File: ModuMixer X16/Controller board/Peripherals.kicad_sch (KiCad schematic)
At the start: 32 parts, among them J1 Screw_Terminal_01x05, J10 Conn_02x05_Counter_Clockwise, J11 Conn_02x06_Counter_Clockwise, J2 Screw_Terminal_01x03, J3 Screw_Terminal_01x05, J4 Screw_Terminal_01x03, J5 Screw_Terminal_01x05, J6 Screw_Terminal_01x05, Q1 MMBT2222A, SW1 Enter, SW10 SW_Push, SW11 SW_Push, SW12 SW_Push, SW13 RotaryEncoder_Switch_MP, SW14 RotaryEncoder_Switch_MP, SW15 RotaryEncoder_Switch_MP, SW16 SW_Push, SW17 SW_Push, SW18 SW_Push, SW19 SW_Push, SW2 Up, SW20 SW_Push, SW21 SW_Push, SW3 Down, SW4 Left, SW5 Right, SW6 RotaryEncoder_Switch_MP, SW7 RotaryEncoder_Switch_MP, SW8 SW_Push, SW9 SW_Push

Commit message: update idk
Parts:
- removed J1, J5, J6: Screw_Terminal_01x05, TerminalBlock:TerminalBlock_Xinya_XY308-2.54-5P_1x05_P2.54mm_Horizontal, symbol Connector:Screw_Terminal_01x05
- removed J4: Screw_Terminal_01x03, TerminalBlock:TerminalBlock_Xinya_XY308-2.54-3P_1x03_P2.54mm_Horizontal, symbol Connector:Screw_Terminal_01x03
- added J5: Conn_02x07_Counter_Clockwise, Connector_IDC:IDC-Header_2x07_P2.54mm_Vertical, symbol Connector_Generic:Conn_02x07_Counter_Clockwise
- added JP10, JP11: SolderJumper_2_Bridged, Jumper:SolderJumper-2_P1.3mm_Bridged2Bar_Pad1.0x1.5mm, symbol Jumper:SolderJumper_2_Bridged
- renumbered J2 to J1, J3 to J2, J10 to J3, J11 to J4
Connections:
- net GND: now also J5.2 (Pin_2)
- net MAIN_OUT_L_P: now also JP10.2 (B)
- net MAIN_OUT_R_P: now also JP11.1 (A)
- net M_USART_CLK: now also J5.6 (Pin_6)
- net M_USART_RX: now also J5.5 (Pin_5)
- net M_USART_TX: now also J5.4 (Pin_4)
- net READY: now also J5.3 (Pin_3)
- new net 12V_MOD: J5.1 (Pin_1)
- new net CUE_LM: J5.10 (Pin_10)
- new net CUE_LP: J5.9 (Pin_9)
- new net CUE_RM: J5.8 (Pin_8)
- new net CUE_RP: J5.7 (Pin_7)
- new net MAIN_LM: J5.14 (Pin_14)
- new net MAIN_LP: J5.13 (Pin_13)
- new net MAIN_RM: J5.12 (Pin_12)
- new net MAIN_RP: J5.11 (Pin_11)
- new net OUT_L_PRE: JP10.1 (A)
- new net OUT_R_PRE: JP11.2 (B)
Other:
- note added: "Headphone output"
- note removed: "Headphone input"
- note removed: "Main input"
- note removed: "Module data terminals"
- note removed: "Module power terminals"

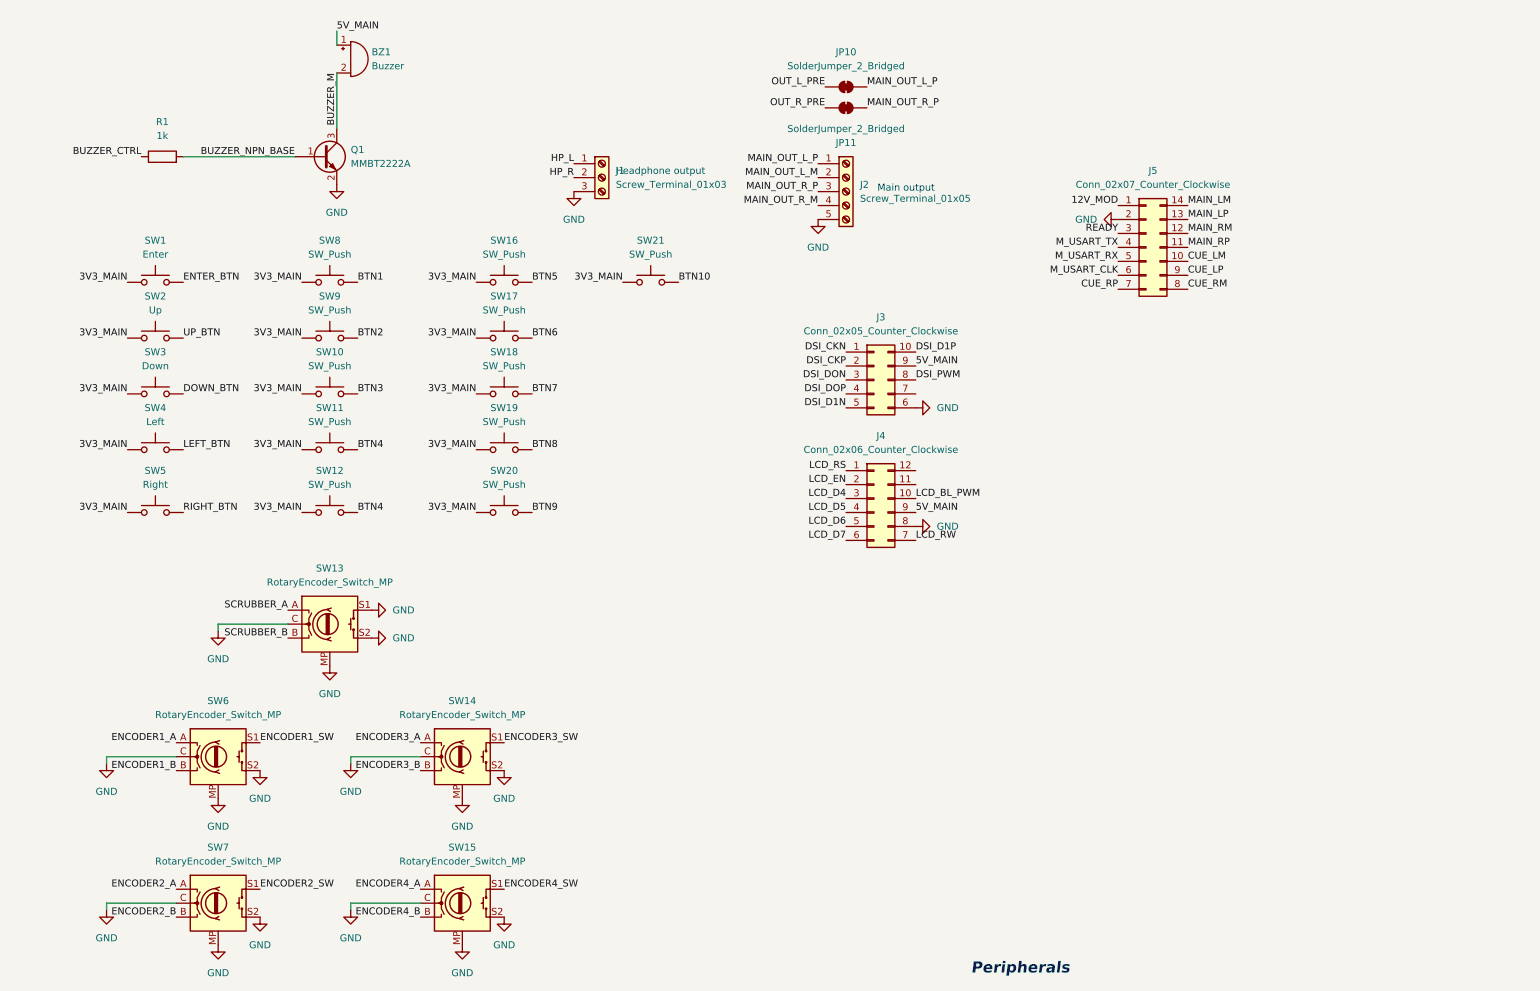
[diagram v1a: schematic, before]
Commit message: Switching microcontrollers
Midway through switching all microcontrollers in the project to STM32F103RC due to price constraints
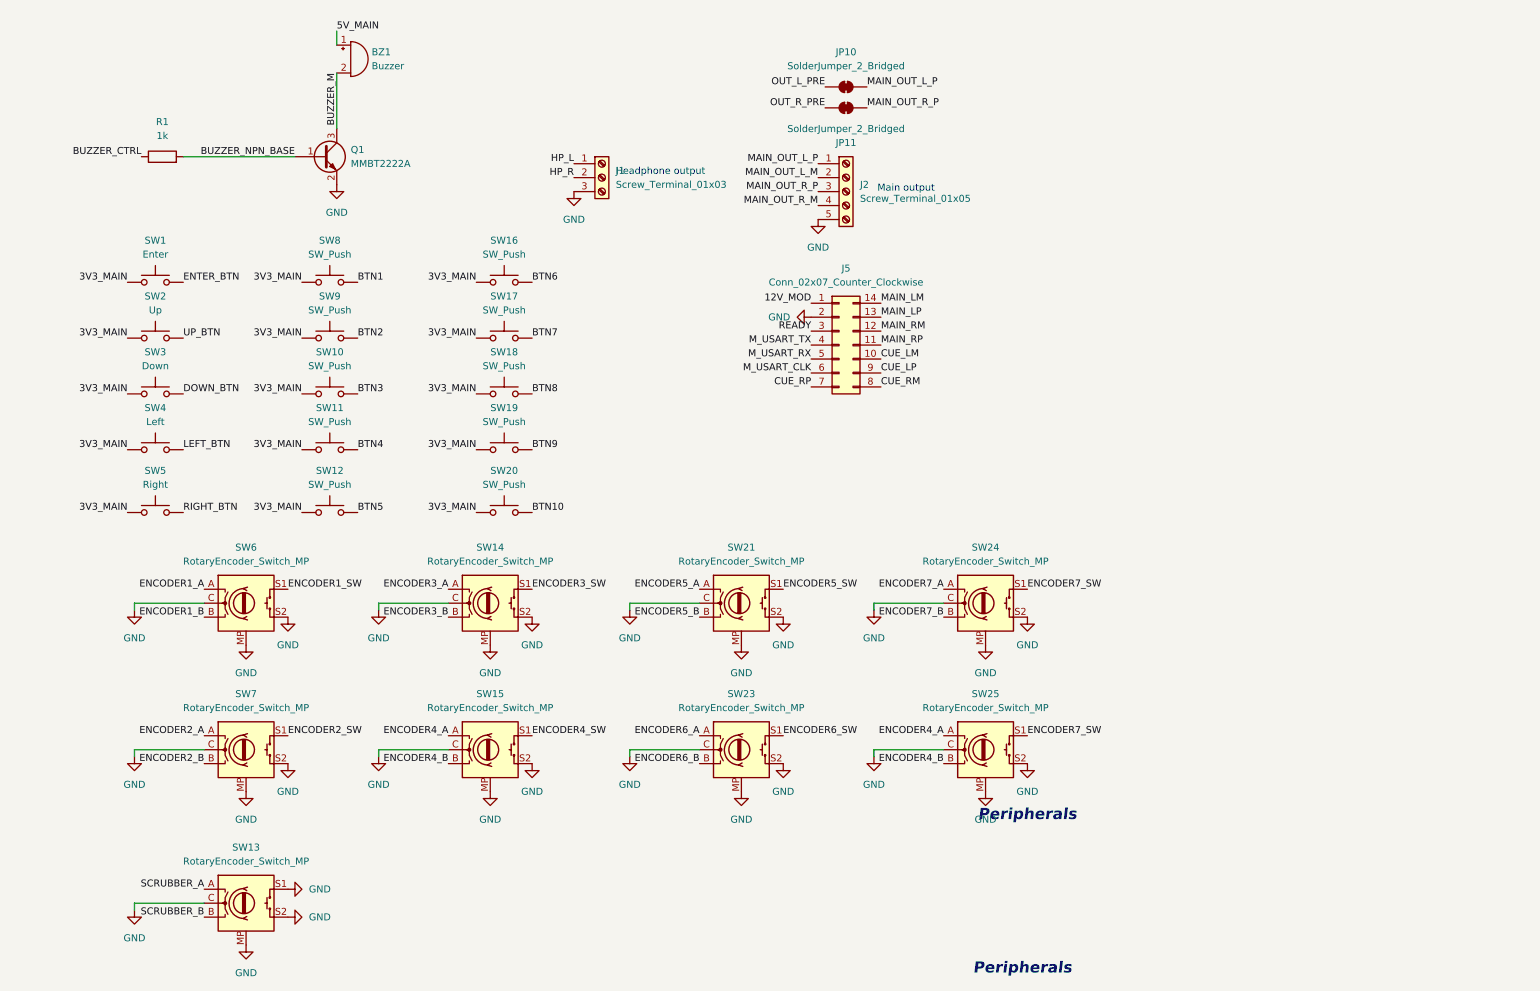
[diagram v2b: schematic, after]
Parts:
- removed J3: Conn_02x05_Counter_Clockwise, Connector_Molex:Molex_Nano-Fit_105310-xx10_2x05_P2.50mm_Vertical, symbol Connector_Generic:Conn_02x05_Counter_Clockwise
- removed J4: Conn_02x06_Counter_Clockwise, Connector_IDC:IDC-Header_2x06_P2.54mm_Vertical, symbol Connector_Generic:Conn_02x06_Counter_Clockwise
- removed SW21: SW_Push, Button_Switch_SMD:SW_SPST_B3S-1000, symbol Switch:SW_Push
- added SW21, SW23, SW24, SW25: RotaryEncoder_Switch_MP, Rotary_Encoder:RotaryEncoder_Alps_EC11E-Switch_Vertical_H20mm, symbol Device:RotaryEncoder_Switch_MP
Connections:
- net BTN10: now also SW20.2
- net BTN4: no longer SW12.2
- net BTN5: now also SW12.2; no longer SW16.2
- net BTN6: now also SW16.2; no longer SW17.2
- net BTN7: now also SW17.2; no longer SW18.2
- net BTN8: now also SW18.2; no longer SW19.2
- net BTN9: now also SW19.2; no longer SW20.2
- net ENCODER4_A: now also SW25.A
- net ENCODER4_B: now also SW25.B
- net GND: now also SW21.C, SW21.MP, SW21.S2, SW23.C, SW23.MP, SW23.S2, SW24.C, SW24.MP, SW24.S2, SW25.C, SW25.MP, SW25.S2
- new net ENCODER5_A: SW21.A
- new net ENCODER5_B: SW21.B
- new net ENCODER5_SW: SW21.S1
- new net ENCODER6_A: SW23.A
- new net ENCODER6_B: SW23.B
- new net ENCODER6_SW: SW23.S1
- new net ENCODER7_A: SW24.A
- new net ENCODER7_B: SW24.B
- new net ENCODER7_SW: SW24.S1, SW25.S1
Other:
- moved on the sheet: J5, SW13, SW14, SW15, SW6, SW7

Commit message: Midway through MCU change
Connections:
- net ENCODER4_A: no longer SW25.A
- net ENCODER4_B: no longer SW25.B
- net ENCODER7_SW: no longer SW25.S1
- new net ENCODER8_A: SW25.A
- new net ENCODER8_B: SW25.B
- new net ENCODER8_SW: SW25.S1
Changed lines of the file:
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@@
-		)
-	)
-	(text "Peripherals"
-		(exclude_from_sim no)
-		(at 195.58 161.798 0)
-		(effects
-			(font
-				(size 2.032 2.032)
-				(thickness 0.4064)
-				(bold yes)
-				(italic yes)
-				(color 132 0 0 1)
-			)
 		)
 	)
@@
 		)
 	)
-	(label "ENCODER4_A"
+	(label "ENCODER8_A"
 		(at 180.34 147.32 180)
 		(fields_autoplaced yes)
@@
 		)
 	)
-	(label "ENCODER4_B"
+	(label "ENCODER8_B"
 		(at 180.34 152.4 180)
 		(fields_autoplaced yes)
@@
 		)
 	)
-	(label "ENCODER7_SW"
+	(label "ENCODER8_SW"
 		(at 195.58 147.32 0)
 		(fields_autoplaced yes)

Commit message: Midway through MCU replacement
Sometimes i feel like it would be better to start over considering it's a digital mixer.
The only thing left is doing the DSP connections and calculating the values for a 16mhz crystal on all 3 MCUs
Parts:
- removed SW12, SW20: SW_Push, Button_Switch_SMD:SW_SPST_B3S-1000, symbol Switch:SW_Push
- removed SW5: Right, Button_Switch_SMD:SW_SPST_B3S-1000, symbol Switch:SW_Push
- added J7: Conn_02x04_Counter_Clockwise, symbol Connector_Generic:Conn_02x04_Counter_Clockwise
- added SW16, SW17, SW18, SW19: SW_Push, Button_Switch_SMD:SW_SPST_B3S-1000, symbol Switch:SW_Push
- SW8: value SW_Push -> Right
- renumbered J5 to J2, J2 to J3, JP10 to JP2, JP11 to JP3, SW16 to SW12, SW17 to SW13, SW18 to SW14, SW19 to SW15, SW14 to SW20, SW15 to SW21, SW21 to SW22, SW6 to SW5, SW7 to SW6, SW13 to SW7
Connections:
- net 3V3_MAIN is gone; now on net GND: SW1.1, SW10.1, SW11.1, SW12.1, SW13.1, SW14.1, SW15.1, SW2.1, SW3.1, SW4.1, SW8.1, SW9.1
- net DOWN_BTN is gone; now on net BTN3: SW3.2
- net ENTER_BTN is gone; now on net BTN1: SW1.2
- net LEFT_BTN is gone; now on net BTN4: SW4.2
- net M_USART_CLK is gone; now on net CUE_RP: J2.6 (Pin_6)
- net UP_BTN is gone; now on net BTN2: SW2.2
- net 5V_MAIN: now also J7.2 (Pin_2)
- net BTN1: no longer SW8.2
- net BTN10: now also SW13.2
- net BTN2: no longer SW9.2
- net BTN3: no longer SW10.2
- net BTN4: no longer SW11.2
- net BTN5: now also SW8.2
- net BTN6: now also SW9.2; no longer SW12.2
- net BTN7: now also SW10.2; no longer SW13.2
- net BTN8: now also SW11.2; no longer SW14.2
- net BTN9: now also SW12.2; no longer SW15.2
- net CUE_LM: now also J2.9 (Pin_9); no longer J2.10 (Pin_10)
- net CUE_LP: now also J2.8 (Pin_8); no longer J2.9 (Pin_9)
- net CUE_RM: now also J2.7 (Pin_7); no longer J2.8 (Pin_8)
- net CUE_RP: no longer J2.7 (Pin_7)
- net GND: now also J7.1 (Pin_1), SW16.1, SW17.1, SW18.1, SW19.1
- net MAIN_LM: now also J2.13 (Pin_13); no longer J2.14 (Pin_14)
- net MAIN_LP: now also J2.12 (Pin_12); no longer J2.13 (Pin_13)
- net MAIN_RM: now also J2.11 (Pin_11); no longer J2.12 (Pin_12)
- net MAIN_RP: now also J2.10 (Pin_10); no longer J2.11 (Pin_11)
- net M_USART_RX renamed MOD_SDA
- net M_USART_TX renamed MOD_SCL
- new net BTN11: SW14.2
- new net BTN12: SW15.2
- new net BTN13: SW16.2
- new net BTN14: SW17.2
- new net BTN15: SW18.2
- new net BTN16: SW19.2
- new net LCD_CLK: J7.5 (Pin_5)
- new net LCD_CS1: J7.3 (Pin_3)
- new net LCD_CS2: J7.4 (Pin_4)
- new net LCD_MISO: J7.6 (Pin_6)
- new net LCD_MOSI: J7.7 (Pin_7)
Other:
- note added: "Both screens will be a 3.5" TFT LCD with a ILI9485 controller on SPI Mode Touchscreen will not be used"
- moved on the sheet: SW1, SW10, SW11, SW12, SW13, SW14, SW15, SW2, SW3, SW4, SW8, SW9

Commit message: MCU replacement done
I finally did everything (i guess), i replaced the MCUs, set the clock components, connected them, idk i guess it's ok now, we just gotta make that pcb
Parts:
- added J8: Conn_02x07_Counter_Clockwise, Connector_IDC:IDC-Header_2x07_P2.54mm_Vertical, symbol Connector_Generic:Conn_02x07_Counter_Clockwise
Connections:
- net GND: now also J8.14 (Pin_14)
- new net 3V3_MAIN: J8.13 (Pin_13)
- new net DSP_BOOT: J8.10 (Pin_10)
- new net DSP_RESET: J8.9 (Pin_9)
- new net DSP_SWDCLK: J8.11 (Pin_11)
- new net DSP_SWIO: J8.12 (Pin_12)
- new net MAIN_BOOT: J8.2 (Pin_2)
- new net MAIN_RESET: J8.1 (Pin_1)
- new net MAIN_SWDCLK: J8.3 (Pin_3)
- new net MAIN_SWDIO: J8.4 (Pin_4)
- new net PERIPHERAL_BOOT: J8.6 (Pin_6)
- new net PERIPHERAL_RESET: J8.5 (Pin_5)
- new net PERIPHERAL_SWDCLK: J8.7 (Pin_7)
- new net PERIPHERAL_SWDIO: J8.8 (Pin_8)
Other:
- note added: "Hidden debug header"

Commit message: asdasgashg
sfjhadgdjasdg
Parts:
- removed J1: Screw_Terminal_01x03, TerminalBlock:TerminalBlock_Xinya_XY308-2.54-3P_1x03_P2.54mm_Horizontal, symbol Connector:Screw_Terminal_01x03
- removed J3: Screw_Terminal_01x05, TerminalBlock:TerminalBlock_Xinya_XY308-2.54-5P_1x05_P2.54mm_Horizontal, symbol Connector:Screw_Terminal_01x05
- added J1: Conn_01x03_Pin, Connector_PinHeader_2.54mm:PinHeader_1x03_P2.54mm_Vertical, symbol Connector:Conn_01x03_Pin
- added J4: Conn_01x05_Pin, Connector_PinSocket_2.54mm:PinSocket_1x05_P2.54mm_Vertical, symbol Connector:Conn_01x05_Pin
- added J8, J9: Conn_02x25_Counter_Clockwise, Connector_IDC:IDC-Header_2x25_P2.54mm_Vertical, symbol Connector_Generic:Conn_02x25_Counter_Clockwise
- J2: renamed from J7; footprint (none) -> Connector_PinSocket_2.54mm:PinSocket_2x04_P2.54mm_Vertical
- renumbered J2 to J3, J8 to J5, JP2 to JP3, JP3 to JP4, R1 to R4
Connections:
- net BTN1: now also J8.27 (Pin_27), J9.27 (Pin_27)
- net BTN10: now also J8.36 (Pin_36), J9.36 (Pin_36)
- net BTN11: now also J8.37 (Pin_37), J9.37 (Pin_37)
- net BTN12: now also J8.38 (Pin_38), J9.38 (Pin_38)
- net BTN13: now also J8.39 (Pin_39), J9.39 (Pin_39)
- net BTN14: now also J8.40 (Pin_40), J9.40 (Pin_40)
- net BTN15: now also J8.41 (Pin_41), J9.41 (Pin_41)
- net BTN16: now also J8.42 (Pin_42), J9.42 (Pin_42)
- net BTN2: now also J8.28 (Pin_28), J9.28 (Pin_28)
- net BTN3: now also J8.29 (Pin_29), J9.29 (Pin_29)
- net BTN4: now also J8.30 (Pin_30), J9.30 (Pin_30)
- net BTN5: now also J8.31 (Pin_31), J9.31 (Pin_31)
- net BTN6: now also J8.32 (Pin_32), J9.32 (Pin_32)
- net BTN7: now also J8.33 (Pin_33), J9.33 (Pin_33)
- net BTN8: now also J8.34 (Pin_34), J9.34 (Pin_34)
- net BTN9: now also J8.35 (Pin_35), J9.35 (Pin_35)
- net ENCODER1_A: now also J8.3 (Pin_3), J9.3 (Pin_3)
- net ENCODER1_B: now also J8.4 (Pin_4), J9.4 (Pin_4)
- net ENCODER1_SW: now also J8.20 (Pin_20), J9.20 (Pin_20)
- net ENCODER2_A: now also J8.5 (Pin_5), J9.5 (Pin_5)
- net ENCODER2_B: now also J8.6 (Pin_6), J9.6 (Pin_6)
- net ENCODER2_SW: now also J8.19 (Pin_19), J9.19 (Pin_19)
- net ENCODER3_A: now also J8.7 (Pin_7), J9.7 (Pin_7)
- net ENCODER3_B: now also J8.8 (Pin_8), J9.8 (Pin_8)
- net ENCODER3_SW: now also J8.21 (Pin_21), J9.21 (Pin_21)
- net ENCODER4_A: now also J8.9 (Pin_9), J9.9 (Pin_9)
- net ENCODER4_B: now also J8.10 (Pin_10), J9.10 (Pin_10)
- net ENCODER4_SW: now also J8.22 (Pin_22), J9.22 (Pin_22)
- net ENCODER5_A: now also J8.11 (Pin_11), J9.11 (Pin_11)
- net ENCODER5_B: now also J8.12 (Pin_12), J9.12 (Pin_12)
- net ENCODER5_SW: now also J8.23 (Pin_23), J9.23 (Pin_23)
- net ENCODER6_A: now also J8.13 (Pin_13), J9.13 (Pin_13)
- net ENCODER6_B: now also J8.14 (Pin_14), J9.14 (Pin_14)
- net ENCODER6_SW: now also J8.24 (Pin_24), J9.24 (Pin_24)
- net ENCODER7_A: now also J8.15 (Pin_15), J9.15 (Pin_15)
- net ENCODER7_B: now also J8.16 (Pin_16), J9.16 (Pin_16)
- net ENCODER7_SW: now also J8.25 (Pin_25), J9.25 (Pin_25)
- net ENCODER8_A: now also J8.17 (Pin_17), J9.17 (Pin_17)
- net ENCODER8_B: now also J8.18 (Pin_18), J9.18 (Pin_18)
- net ENCODER8_SW: now also J8.26 (Pin_26), J9.26 (Pin_26)
- net GND: now also J1.3 (Pin_3), J4.5 (Pin_5), J8.43 (Pin_43), J8.44 (Pin_44), J8.45 (Pin_45), J9.43 (Pin_43), J9.44 (Pin_44), J9.45 (Pin_45)
- net HP_L: now also J1.1 (Pin_1)
- net HP_R: now also J1.2 (Pin_2)
- net MAIN_OUT_L_M: now also J4.2 (Pin_2)
- net MAIN_OUT_L_P: now also J4.1 (Pin_1)
- net MAIN_OUT_R_M: now also J4.4 (Pin_4)
- net MAIN_OUT_R_P: now also J4.3 (Pin_3)
- net SCRUBBER_A: now also J8.1 (Pin_1), J9.1 (Pin_1)
- net SCRUBBER_B: now also J8.2 (Pin_2), J9.2 (Pin_2)
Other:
- moved on the sheet: BZ1, J2, J3, J5, JP3, JP4, Q1, R4, SW1, SW10, SW11, SW12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
